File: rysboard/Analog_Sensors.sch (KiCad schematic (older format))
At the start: 25 parts, among them J14 BAT2_TH, J21 BAT3_TH, J8 BAT1_TH, Q10 DMP2075UFDB

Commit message: more footprints
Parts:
- gave numbers to parts that had none: 4
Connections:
- net BOARD_T_2 renamed CHASSIS_T_2
- net BOARD_T_3 renamed CHASSIS_T_1
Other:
- moved on the sheet: J22, J23, R59, R61
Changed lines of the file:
@@
 Text HLabel 2500 2525 0    50   Input ~ 0
 BOARD_T_1
-Text HLabel 4975 1300 0    50   Input ~ 0
-BOARD_T_2
+Text HLabel 6475 2650 0    50   Input ~ 0
+CHASSIS_T_2
 Text HLabel 1700 4550 0    50   Input ~ 0
 V_P_20
@@
 	1    0    0    1
 $EndComp
-Text Label 4325 900  0    50   ~ 0
-MCU_Sensor_3.3V
-Text Label 5100 900  0    50   ~ 0
-MCU_Sensor_3.3V
-$Comp
-L Device:R R?
+Text Label 5825 2250 0    50   ~ 0
+MCU_Sensor_3.3V
+Text Label 4750 2250 0    50   ~ 0
+MCU_Sensor_3.3V
+$Comp
+L Device:R R61
 U 1 1 604C3349
-P 4975 1050
-F 0 "R?" H 5045 1096 50  0000 L CNN
-F 1 "10KR" H 5045 1005 50  0000 L CNN
-F 2 "Resistor_SMD:R_0603_1608Metric" V 4905 1050 50  0001 C CNN
-F 3 "~" H 4975 1050 50  0001 C CNN
-	1    4975 1050
-	1    0    0    -1
-$EndComp
-$Comp
-L Connector_Generic:Conn_01x02 J?
+P 6475 2400
+F 0 "R61" H 6545 2446 50  0000 L CNN
+F 1 "10KR" H 6545 2355 50  0000 L CNN
+F 2 "Resistor_SMD:R_0603_1608Metric" V 6405 2400 50  0001 C CNN
+F 3 "~" H 6475 2400 50  0001 C CNN
+	1    6475 2400
+	1    0    0    -1
+$EndComp
+$Comp
+L Connector_Generic:Conn_01x02 J23
 U 1 1 604C3809
-P 5075 1550
-F 0 "J?" V 4947 1630 50  0000 L CNN
-F 1 "BAT2_TH" V 5038 1630 50  0000 L CNN
-F 2 "" H 5075 1550 50  0001 C CNN
-F 3 "~" H 5075 1550 50  0001 C CNN
-	1    5075 1550
+P 6575 2900
+F 0 "J23" V 6447 2980 50  0000 L CNN
+F 1 "BAT2_TH" V 6538 2980 50  0000 L CNN
+F 2 "" H 6575 2900 50  0001 C CNN
+F 3 "~" H 6575 2900 50  0001 C CNN
+	1    6575 2900
 	0    1    1    0
 $EndComp
 $Comp
-L Connector_Generic:Conn_01x02 J?
+L Connector_Generic:Conn_01x02 J22
 U 1 1 604C3EA4
-P 5850 1550
-F 0 "J?" V 5722 1630 50  0000 L CNN
-F 1 "BAT2_TH" V 5813 1630 50  0000 L CNN
-F 2 "" H 5850 1550 50  0001 C CNN
-F 3 "~" H 5850 1550 50  0001 C CNN
-	1    5850 1550
+P 5500 2900
+F 0 "J22" V 5372 2980 50  0000 L CNN
+F 1 "BAT2_TH" V 5463 2980 50  0000 L CNN
+F 2 "" H 5500 2900 50  0001 C CNN
+F 3 "~" H 5500 2900 50  0001 C CNN
+	1    5500 2900
 	0    1    1    0
 $EndComp
 $Comp
-L Device:R R?
+L Device:R R59
 U 1 1 604C4170
-P 5750 1050
-F 0 "R?" H 5820 1096 50  0000 L CNN
-F 1 "10KR" H 5820 1005 50  0000 L CNN
-F 2 "Resistor_SMD:R_0603_1608Metric" V 5680 1050 50  0001 C CNN
-F 3 "~" H 5750 1050 50  0001 C CNN
-	1    5750 1050
-	1    0    0    -1
-$EndComp
-Wire Wire Line
-	5100 900  5750 900
-Wire Wire Line
-	4325 900  4975 900
-Wire Wire Line
-	4975 1200 4975 1350
-Text HLabel 5750 1275 0    50   Input ~ 0
-BOARD_T_3
-Wire Wire Line
-	5750 1200 5750 1350
-$Comp
-L power:GND #PWR?
+P 5400 2400
+F 0 "R59" H 5470 2446 50  0000 L CNN
+F 1 "10KR" H 5470 2355 50  0000 L CNN
+F 2 "Resistor_SMD:R_0603_1608Metric" V 5330 2400 50  0001 C CNN
+F 3 "~" H 5400 2400 50  0001 C CNN
+	1    5400 2400
+	1    0    0    -1
+$EndComp
+Wire Wire Line
+	4750 2250 5400 2250
+Wire Wire Line
+	5825 2250 6475 2250
+Wire Wire Line
+	6475 2550 6475 2700
+Text HLabel 5400 2625 0    50   Input ~ 0
+CHASSIS_T_1
+Wire Wire Line
+	5400 2550 5400 2700
+$Comp
+L power:GND #PWR0108
 U 1 1 604C7572
-P 5075 1350
-F 0 "#PWR?" H 5075 1100 50  0001 C CNN
-F 1 "GND" H 5080 1177 50  0000 C CNN
-F 2 "" H 5075 1350 50  0001 C CNN
-F 3 "" H 5075 1350 50  0001 C CNN
-	1    5075 1350
+P 6575 2700
+F 0 "#PWR0108" H 6575 2450 50  0001 C CNN
+F 1 "GND" H 6580 2527 50  0000 C CNN
+F 2 "" H 6575 2700 50  0001 C CNN
+F 3 "" H 6575 2700 50  0001 C CNN
+	1    6575 2700
 	0    -1   -1   0
 $EndComp
 $Comp
-L power:GND #PWR?
+L power:GND #PWR0109
 U 1 1 604C77C4
-P 5850 1350
-F 0 "#PWR?" H 5850 1100 50  0001 C CNN
-F 1 "GND" H 5855 1177 50  0000 C CNN
-F 2 "" H 5850 1350 50  0001 C CNN
-F 3 "" H 5850 1350 50  0001 C CNN
-	1    5850 1350
+P 5500 2700
+F 0 "#PWR0109" H 5500 2450 50  0001 C CNN
+F 1 "GND" H 5505 2527 50  0000 C CNN
+F 2 "" H 5500 2700 50  0001 C CNN
+F 3 "" H 5500 2700 50  0001 C CNN
+	1    5500 2700
 	0    -1   -1   0
 $EndComp

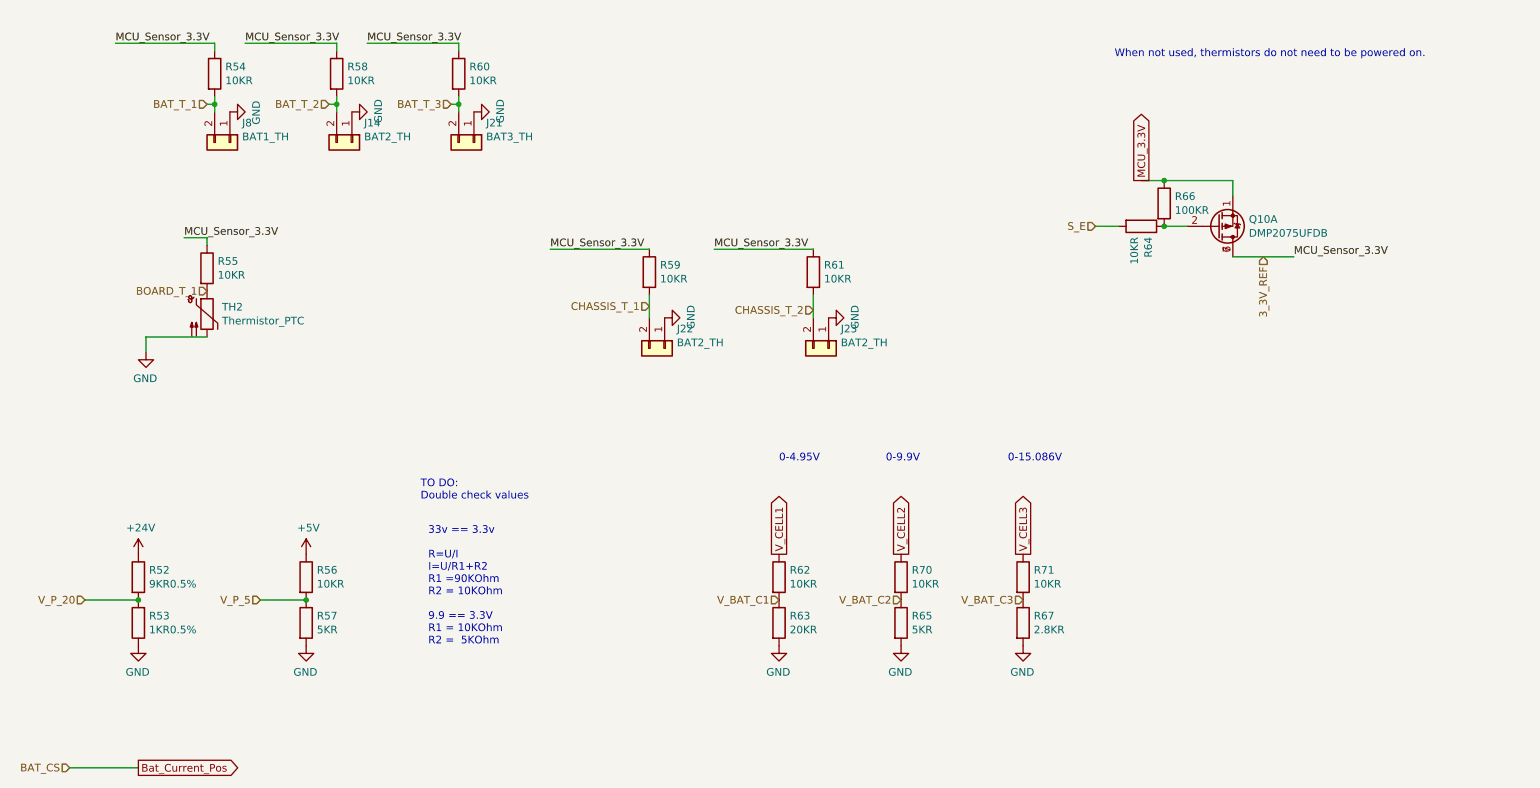
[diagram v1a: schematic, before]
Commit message: LTC4007 done
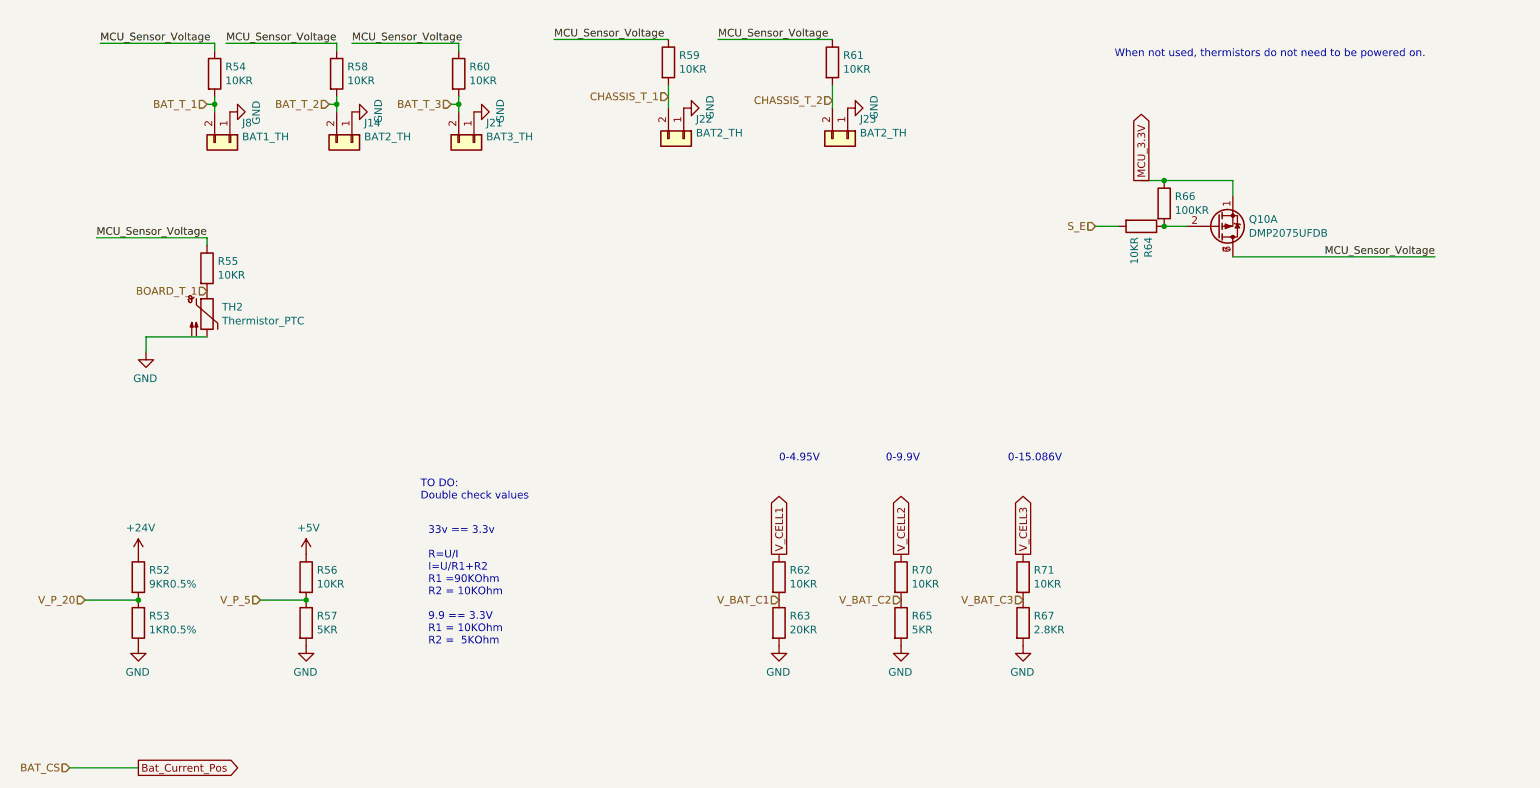
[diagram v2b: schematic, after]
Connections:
- net 3_3V_REF renamed MCU_Sensor_Voltage
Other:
- moved on the sheet: J22, J23, R59, R61
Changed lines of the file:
@@
 Text HLabel 2500 2525 0    50   Input ~ 0
 BOARD_T_1
-Text HLabel 6475 2650 0    50   Input ~ 0
+Text HLabel 6600 1275 0    50   Input ~ 0
 CHASSIS_T_2
 Text HLabel 1700 4550 0    50   Input ~ 0
@@
 $EndComp
 Wire Wire Line
-	2350 2175 2500 2175
-Wire Wire Line
 	2500 2175 2500 2225
 $Comp
@@
 Text GLabel 8625 1800 1    50   Output ~ 0
 MCU_3.3V
-Text Label 2350 2175 0    50   ~ 0
-MCU_Sensor_3.3V
-Text Label 1900 900  0    50   ~ 0
-MCU_Sensor_3.3V
-Wire Wire Line
-	1900 900  2550 900
 Wire Wire Line
 	2550 900  2550 950
-Text Label 2750 900  0    50   ~ 0
-MCU_Sensor_3.3V
-Wire Wire Line
-	2750 900  3350 900
 Wire Wire Line
 	3350 900  3350 950
-Text Label 3550 900  0    50   ~ 0
-MCU_Sensor_3.3V
-Wire Wire Line
-	3550 900  4150 900
 Wire Wire Line
 	4150 900  4150 950
-Text Label 9625 2300 0    50   ~ 0
-MCU_Sensor_3.3V
+Text Label 10550 2300 2    50   ~ 0
+MCU_Sensor_Voltage
 $Comp
 L Device:R R55
@@
 	1    0    0    -1
 $EndComp
-Wire Wire Line
-	9625 2300 9225 2300
 Wire Wire Line
 	8625 1800 8775 1800
@@
 	1    0    0    -1
 $EndComp
-Text HLabel 9425 2300 3    50   Input ~ 0
-3_3V_REF
 $Comp
 L rysboard:DMP2075UFDB Q10
@@
 	1    0    0    1
 $EndComp
-Text Label 5825 2250 0    50   ~ 0
-MCU_Sensor_3.3V
-Text Label 4750 2250 0    50   ~ 0
-MCU_Sensor_3.3V
 $Comp
 L Device:R R61
 U 1 1 604C3349
-P 6475 2400
-F 0 "R61" H 6545 2446 50  0000 L CNN
-F 1 "10KR" H 6545 2355 50  0000 L CNN
-F 2 "Resistor_SMD:R_0603_1608Metric" V 6405 2400 50  0001 C CNN
-F 3 "~" H 6475 2400 50  0001 C CNN
-	1    6475 2400
+P 6600 1025
+F 0 "R61" H 6670 1071 50  0000 L CNN
+F 1 "10KR" H 6670 980 50  0000 L CNN
+F 2 "Resistor_SMD:R_0603_1608Metric" V 6530 1025 50  0001 C CNN
+F 3 "~" H 6600 1025 50  0001 C CNN
+	1    6600 1025
 	1    0    0    -1
 $EndComp
@@
 L Connector_Generic:Conn_01x02 J23
 U 1 1 604C3809
-P 6575 2900
-F 0 "J23" V 6447 2980 50  0000 L CNN
-F 1 "BAT2_TH" V 6538 2980 50  0000 L CNN
-F 2 "" H 6575 2900 50  0001 C CNN
-F 3 "~" H 6575 2900 50  0001 C CNN
-	1    6575 2900
+P 6700 1525
+F 0 "J23" V 6572 1605 50  0000 L CNN
+F 1 "BAT2_TH" V 6663 1605 50  0000 L CNN
+F 2 "" H 6700 1525 50  0001 C CNN
+F 3 "~" H 6700 1525 50  0001 C CNN
+	1    6700 1525
 	0    1    1    0
 $EndComp
@@
 L Connector_Generic:Conn_01x02 J22
 U 1 1 604C3EA4
-P 5500 2900
-F 0 "J22" V 5372 2980 50  0000 L CNN
-F 1 "BAT2_TH" V 5463 2980 50  0000 L CNN
-F 2 "" H 5500 2900 50  0001 C CNN
-F 3 "~" H 5500 2900 50  0001 C CNN
-	1    5500 2900
+P 5625 1525
+F 0 "J22" V 5497 1605 50  0000 L CNN
+F 1 "BAT2_TH" V 5588 1605 50  0000 L CNN
+F 2 "" H 5625 1525 50  0001 C CNN
+F 3 "~" H 5625 1525 50  0001 C CNN
+	1    5625 1525
 	0    1    1    0
 $EndComp
@@
 L Device:R R59
 U 1 1 604C4170
-P 5400 2400
-F 0 "R59" H 5470 2446 50  0000 L CNN
-F 1 "10KR" H 5470 2355 50  0000 L CNN
-F 2 "Resistor_SMD:R_0603_1608Metric" V 5330 2400 50  0001 C CNN
-F 3 "~" H 5400 2400 50  0001 C CNN
-	1    5400 2400
-	1    0    0    -1
-$EndComp
-Wire Wire Line
-	4750 2250 5400 2250
-Wire Wire Line
-	5825 2250 6475 2250
-Wire Wire Line
-	6475 2550 6475 2700
-Text HLabel 5400 2625 0    50   Input ~ 0
+P 5525 1025
+F 0 "R59" H 5595 1071 50  0000 L CNN
+F 1 "10KR" H 5595 980 50  0000 L CNN
+F 2 "Resistor_SMD:R_0603_1608Metric" V 5455 1025 50  0001 C CNN
+F 3 "~" H 5525 1025 50  0001 C CNN
+	1    5525 1025
+	1    0    0    -1
+$EndComp
+Wire Wire Line
+	6600 1175 6600 1325
+Text HLabel 5525 1250 0    50   Input ~ 0
 CHASSIS_T_1
 Wire Wire Line
-	5400 2550 5400 2700
+	5525 1175 5525 1325
 $Comp
 L power:GND #PWR0108
 U 1 1 604C7572
-P 6575 2700
-F 0 "#PWR0108" H 6575 2450 50  0001 C CNN
-F 1 "GND" H 6580 2527 50  0000 C CNN
-F 2 "" H 6575 2700 50  0001 C CNN
-F 3 "" H 6575 2700 50  0001 C CNN
-	1    6575 2700
+P 6700 1325
+F 0 "#PWR0108" H 6700 1075 50  0001 C CNN
+F 1 "GND" H 6705 1152 50  0000 C CNN
+F 2 "" H 6700 1325 50  0001 C CNN
+F 3 "" H 6700 1325 50  0001 C CNN
+	1    6700 1325
 	0    -1   -1   0
 $EndComp
@@
 L power:GND #PWR0109
 U 1 1 604C77C4
-P 5500 2700
-F 0 "#PWR0109" H 5500 2450 50  0001 C CNN
-F 1 "GND" H 5505 2527 50  0000 C CNN
-F 2 "" H 5500 2700 50  0001 C CNN
-F 3 "" H 5500 2700 50  0001 C CNN
-	1    5500 2700
+P 5625 1325
+F 0 "#PWR0109" H 5625 1075 50  0001 C CNN
+F 1 "GND" H 5630 1152 50  0000 C CNN
+F 2 "" H 5625 1325 50  0001 C CNN
+F 3 "" H 5625 1325 50  0001 C CNN
+	1    5625 1325
 	0    -1   -1   0
 $EndComp
+Text Label 1800 900  0    50   ~ 0
+MCU_Sensor_Voltage
+Text Label 2625 900  0    50   ~ 0
+MCU_Sensor_Voltage
+Text Label 3450 900  0    50   ~ 0
+MCU_Sensor_Voltage
+Text Label 4775 875  0    50   ~ 0
+MCU_Sensor_Voltage
+Text Label 5850 875  0    50   ~ 0
+MCU_Sensor_Voltage
+Wire Wire Line
+	5850 875  6600 875
+Wire Wire Line
+	4775 875  5525 875
+Wire Wire Line
+	3450 900  4150 900
+Wire Wire Line
+	2625 900  3350 900
+Wire Wire Line
+	1800 900  2550 900
+Text Label 1775 2175 0    50   ~ 0
+MCU_Sensor_Voltage
+Wire Wire Line
+	1775 2175 2500 2175
+Wire Wire Line
+	9225 2300 10550 2300
 $EndSCHEMATC

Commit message: Even More footprints
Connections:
- net MCU_Sensor_Voltage renamed MCU_ANALOG_SENSOR_V
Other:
- moved on the sheet: J14, J22, J23, J8, R54, R58, R59, R61
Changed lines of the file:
@@
 Comment4 ""
 $EndDescr
-Text HLabel 3300 1300 0    50   Input ~ 0
+Text HLabel 3325 1300 0    50   Input ~ 0
 BAT_T_2
 Text HLabel 4100 1300 0    50   Input ~ 0
@@
 Text HLabel 2500 2525 0    50   Input ~ 0
 BOARD_T_1
-Text HLabel 6600 1275 0    50   Input ~ 0
+Text HLabel 6150 1275 0    50   Input ~ 0
 CHASSIS_T_2
 Text HLabel 1700 4550 0    50   Input ~ 0
@@
 L Connector_Generic:Conn_01x02 J8
 U 1 1 603EB5C9
-P 2650 1550
-F 0 "J8" V 2522 1630 50  0000 L CNN
-F 1 "BAT1_TH" V 2613 1630 50  0000 L CNN
-F 2 "" H 2650 1550 50  0001 C CNN
-F 3 "~" H 2650 1550 50  0001 C CNN
-	1    2650 1550
+P 2500 1550
+F 0 "J8" V 2372 1630 50  0000 L CNN
+F 1 "BAT1_TH" V 2463 1630 50  0000 L CNN
+F 2 "" H 2500 1550 50  0001 C CNN
+F 3 "~" H 2500 1550 50  0001 C CNN
+	1    2500 1550
 	0    1    1    0
 $EndComp
@@
 L Connector_Generic:Conn_01x02 J14
 U 1 1 603EBF1A
-P 3450 1550
-F 0 "J14" V 3322 1630 50  0000 L CNN
-F 1 "BAT2_TH" V 3413 1630 50  0000 L CNN
-F 2 "" H 3450 1550 50  0001 C CNN
-F 3 "~" H 3450 1550 50  0001 C CNN
-	1    3450 1550
+P 3475 1550
+F 0 "J14" V 3347 1630 50  0000 L CNN
+F 1 "BAT2_TH" V 3438 1630 50  0000 L CNN
+F 2 "" H 3475 1550 50  0001 C CNN
+F 3 "~" H 3475 1550 50  0001 C CNN
+	1    3475 1550
 	0    1    1    0
 $EndComp
@@
 L power:GND #PWR050
 U 1 1 603ED9D9
-P 2650 1350
-F 0 "#PWR050" H 2650 1100 50  0001 C CNN
-F 1 "GND" H 2655 1177 50  0000 C CNN
-F 2 "" H 2650 1350 50  0001 C CNN
-F 3 "" H 2650 1350 50  0001 C CNN
-	1    2650 1350
+P 2500 1350
+F 0 "#PWR050" H 2500 1100 50  0001 C CNN
+F 1 "GND" H 2505 1177 50  0000 C CNN
+F 2 "" H 2500 1350 50  0001 C CNN
+F 3 "" H 2500 1350 50  0001 C CNN
+	1    2500 1350
 	0    -1   1    0
 $EndComp
@@
 L power:GND #PWR053
 U 1 1 603EDE43
-P 3450 1350
-F 0 "#PWR053" H 3450 1100 50  0001 C CNN
-F 1 "GND" H 3455 1177 50  0000 C CNN
-F 2 "" H 3450 1350 50  0001 C CNN
-F 3 "" H 3450 1350 50  0001 C CNN
-	1    3450 1350
+P 3475 1350
+F 0 "#PWR053" H 3475 1100 50  0001 C CNN
+F 1 "GND" H 3480 1177 50  0000 C CNN
+F 2 "" H 3475 1350 50  0001 C CNN
+F 3 "" H 3475 1350 50  0001 C CNN
+	1    3475 1350
 	0    -1   -1   0
 $EndComp
@@
 Text Notes 7750 3650 0    50   ~ 0
 0-15.086V\n
-Text HLabel 2500 1300 0    50   Input ~ 0
+Text HLabel 2350 1300 0    50   Input ~ 0
 BAT_T_1
 Wire Wire Line
-	2500 1300 2550 1300
-Wire Wire Line
-	2550 1300 2550 1350
-Wire Wire Line
-	2550 1300 2550 1250
-Connection ~ 2550 1300
-Wire Wire Line
-	3300 1300 3350 1300
-Wire Wire Line
-	3350 1300 3350 1250
-Wire Wire Line
-	3350 1300 3350 1350
-Connection ~ 3350 1300
+	2350 1300 2400 1300
+Wire Wire Line
+	2400 1300 2400 1350
+Wire Wire Line
+	2400 1300 2400 1250
+Connection ~ 2400 1300
+Wire Wire Line
+	3325 1300 3375 1300
+Wire Wire Line
+	3375 1300 3375 1250
+Wire Wire Line
+	3375 1300 3375 1350
+Connection ~ 3375 1300
 Wire Wire Line
 	4100 1300 4150 1300
@@
 MCU_3.3V
 Wire Wire Line
-	2550 900  2550 950
-Wire Wire Line
-	3350 900  3350 950
+	2400 900  2400 950
 Wire Wire Line
 	4150 900  4150 950
-Text Label 10550 2300 2    50   ~ 0
-MCU_Sensor_Voltage
 $Comp
 L Device:R R55
@@
 L Device:R R54
 U 1 1 603FD549
-P 2550 1100
-F 0 "R54" H 2620 1146 50  0000 L CNN
-F 1 "10KR" H 2620 1055 50  0000 L CNN
-F 2 "Resistor_SMD:R_0603_1608Metric" V 2480 1100 50  0001 C CNN
-F 3 "~" H 2550 1100 50  0001 C CNN
-	1    2550 1100
+P 2400 1100
+F 0 "R54" H 2470 1146 50  0000 L CNN
+F 1 "10KR" H 2470 1055 50  0000 L CNN
+F 2 "Resistor_SMD:R_0603_1608Metric" V 2330 1100 50  0001 C CNN
+F 3 "~" H 2400 1100 50  0001 C CNN
+	1    2400 1100
 	1    0    0    -1
 $EndComp
@@
 L Device:R R58
 U 1 1 603FD808
-P 3350 1100
-F 0 "R58" H 3420 1146 50  0000 L CNN
-F 1 "10KR" H 3420 1055 50  0000 L CNN
-F 2 "Resistor_SMD:R_0603_1608Metric" V 3280 1100 50  0001 C CNN
-F 3 "~" H 3350 1100 50  0001 C CNN
-	1    3350 1100
+P 3375 1100
+F 0 "R58" H 3445 1146 50  0000 L CNN
+F 1 "10KR" H 3445 1055 50  0000 L CNN
+F 2 "Resistor_SMD:R_0603_1608Metric" V 3305 1100 50  0001 C CNN
+F 3 "~" H 3375 1100 50  0001 C CNN
+	1    3375 1100
 	1    0    0    -1
 $EndComp
@@
 L Device:R R61
 U 1 1 604C3349
-P 6600 1025
-F 0 "R61" H 6670 1071 50  0000 L CNN
-F 1 "10KR" H 6670 980 50  0000 L CNN
-F 2 "Resistor_SMD:R_0603_1608Metric" V 6530 1025 50  0001 C CNN
-F 3 "~" H 6600 1025 50  0001 C CNN
-	1    6600 1025
+P 6150 1075
+F 0 "R61" H 6220 1121 50  0000 L CNN
+F 1 "10KR" H 6220 1030 50  0000 L CNN
+F 2 "Resistor_SMD:R_0603_1608Metric" V 6080 1075 50  0001 C CNN
+F 3 "~" H 6150 1075 50  0001 C CNN
+	1    6150 1075
 	1    0    0    -1
 $EndComp
@@
 L Connector_Generic:Conn_01x02 J23
 U 1 1 604C3809
-P 6700 1525
-F 0 "J23" V 6572 1605 50  0000 L CNN
-F 1 "BAT2_TH" V 6663 1605 50  0000 L CNN
-F 2 "" H 6700 1525 50  0001 C CNN
-F 3 "~" H 6700 1525 50  0001 C CNN
-	1    6700 1525
+P 6250 1575
+F 0 "J23" V 6122 1655 50  0000 L CNN
+F 1 "BAT2_TH" V 6213 1655 50  0000 L CNN
+F 2 "" H 6250 1575 50  0001 C CNN
+F 3 "~" H 6250 1575 50  0001 C CNN
+	1    6250 1575
 	0    1    1    0
 $EndComp
@@
 L Connector_Generic:Conn_01x02 J22
 U 1 1 604C3EA4
-P 5625 1525
-F 0 "J22" V 5497 1605 50  0000 L CNN
-F 1 "BAT2_TH" V 5588 1605 50  0000 L CNN
-F 2 "" H 5625 1525 50  0001 C CNN
-F 3 "~" H 5625 1525 50  0001 C CNN
-	1    5625 1525
+P 5350 1550
+F 0 "J22" V 5222 1630 50  0000 L CNN
+F 1 "BAT2_TH" V 5313 1630 50  0000 L CNN
+F 2 "" H 5350 1550 50  0001 C CNN
+F 3 "~" H 5350 1550 50  0001 C CNN
+	1    5350 1550
 	0    1    1    0
 $EndComp
@@
 L Device:R R59
 U 1 1 604C4170
-P 5525 1025
-F 0 "R59" H 5595 1071 50  0000 L CNN
-F 1 "10KR" H 5595 980 50  0000 L CNN
-F 2 "Resistor_SMD:R_0603_1608Metric" V 5455 1025 50  0001 C CNN
-F 3 "~" H 5525 1025 50  0001 C CNN
-	1    5525 1025
-	1    0    0    -1
-$EndComp
-Wire Wire Line
-	6600 1175 6600 1325
-Text HLabel 5525 1250 0    50   Input ~ 0
+P 5250 1050
+F 0 "R59" H 5320 1096 50  0000 L CNN
+F 1 "10KR" H 5320 1005 50  0000 L CNN
+F 2 "Resistor_SMD:R_0603_1608Metric" V 5180 1050 50  0001 C CNN
+F 3 "~" H 5250 1050 50  0001 C CNN
+	1    5250 1050
+	1    0    0    -1
+$EndComp
+Wire Wire Line
+	6150 1225 6150 1375
+Text HLabel 5250 1275 0    50   Input ~ 0
 CHASSIS_T_1
 Wire Wire Line
-	5525 1175 5525 1325
+	5250 1200 5250 1350
 $Comp
 L power:GND #PWR0108
 U 1 1 604C7572
-P 6700 1325
-F 0 "#PWR0108" H 6700 1075 50  0001 C CNN
-F 1 "GND" H 6705 1152 50  0000 C CNN
-F 2 "" H 6700 1325 50  0001 C CNN
-F 3 "" H 6700 1325 50  0001 C CNN
-	1    6700 1325
+P 6250 1375
+F 0 "#PWR0108" H 6250 1125 50  0001 C CNN
+F 1 "GND" H 6255 1202 50  0000 C CNN
+F 2 "" H 6250 1375 50  0001 C CNN
+F 3 "" H 6250 1375 50  0001 C CNN
+	1    6250 1375
 	0    -1   -1   0
 $EndComp
@@
 L power:GND #PWR0109
 U 1 1 604C77C4
-P 5625 1325
-F 0 "#PWR0109" H 5625 1075 50  0001 C CNN
-F 1 "GND" H 5630 1152 50  0000 C CNN
-F 2 "" H 5625 1325 50  0001 C CNN
-F 3 "" H 5625 1325 50  0001 C CNN
-	1    5625 1325
+P 5350 1350
+F 0 "#PWR0109" H 5350 1100 50  0001 C CNN
+F 1 "GND" H 5355 1177 50  0000 C CNN
+F 2 "" H 5350 1350 50  0001 C CNN
+F 3 "" H 5350 1350 50  0001 C CNN
+	1    5350 1350
 	0    -1   -1   0
 $EndComp
-Text Label 1800 900  0    50   ~ 0
-MCU_Sensor_Voltage
-Text Label 2625 900  0    50   ~ 0
-MCU_Sensor_Voltage
-Text Label 3450 900  0    50   ~ 0
-MCU_Sensor_Voltage
-Text Label 4775 875  0    50   ~ 0
-MCU_Sensor_Voltage
-Text Label 5850 875  0    50   ~ 0
-MCU_Sensor_Voltage
-Wire Wire Line
-	5850 875  6600 875
-Wire Wire Line
-	4775 875  5525 875
-Wire Wire Line
-	3450 900  4150 900
-Wire Wire Line
-	2625 900  3350 900
-Wire Wire Line
-	1800 900  2550 900
-Text Label 1775 2175 0    50   ~ 0
-MCU_Sensor_Voltage
-Wire Wire Line
-	1775 2175 2500 2175
-Wire Wire Line
-	9225 2300 10550 2300
+Text GLabel 9850 2300 2    50   Input ~ 0
+MCU_ANALOG_SENSOR_V
+Wire Wire Line
+	9850 2300 9225 2300
+Text GLabel 6150 925  2    50   Input ~ 0
+MCU_ANALOG_SENSOR_V
+Text GLabel 5250 750  2    50   Input ~ 0
+MCU_ANALOG_SENSOR_V
+Text GLabel 4150 900  2    50   Input ~ 0
+MCU_ANALOG_SENSOR_V
+Text GLabel 3375 750  2    50   Input ~ 0
+MCU_ANALOG_SENSOR_V
+Wire Wire Line
+	3375 750  3375 950
+Text GLabel 2400 900  2    50   Input ~ 0
+MCU_ANALOG_SENSOR_V
+Wire Wire Line
+	5250 750  5250 900
+Text GLabel 2500 2175 0    50   Input ~ 0
+MCU_ANALOG_SENSOR_V
 $EndSCHEMATC
